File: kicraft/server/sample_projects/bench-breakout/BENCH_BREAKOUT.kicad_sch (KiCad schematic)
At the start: 0 parts

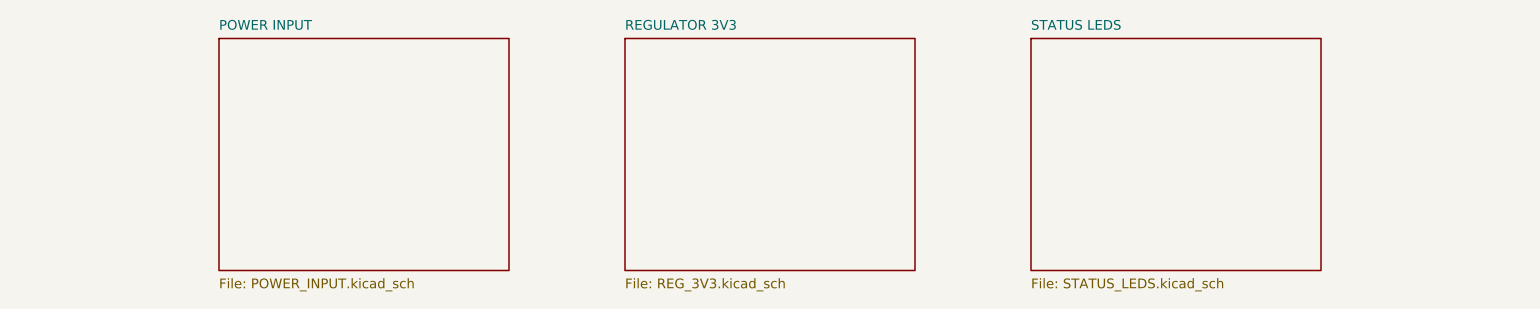
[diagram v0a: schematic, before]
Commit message: feat(showcase): refresh landing samples from self-eval 20260614
Promote the three best boards from self-eval batch 20260614T215540Z
(all grade B) into the landing-page showcase, replacing the regressed
PIR night light (D/45, hit erc_errors + unprogrammable_mcu gates):

- usb-pd-trigger (NEW, featured hero) — 81.0, fab-ready
- weather-sensor (re-promoted; stem A_BMP280_BAROMETRIC -> BMP280_QWIIC_USB_C)
- bench-breakout (re-promoted; 4->5 sheets, 16->19 parts)

Regenerated board.png/hero.png renders and interactive board.glb models
via scripts/promote_to_sample.py. Already live (deploy/restart-web.sh).

Co-Authored-By: Claude Opus 4.8 (1M context) <noreply@anthropic.com>
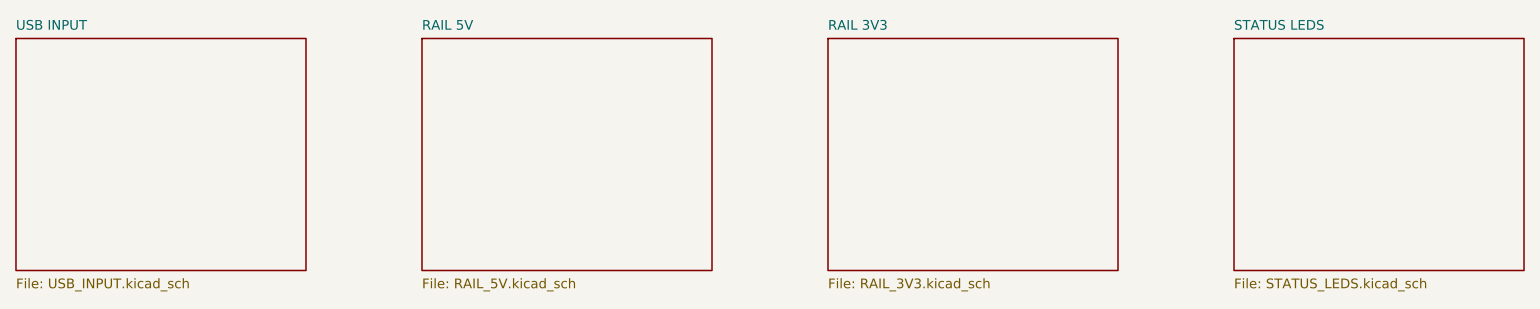
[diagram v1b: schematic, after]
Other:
- removed sheet POWER INPUT
- removed sheet REGULATOR 3V3
- added sheet RAIL 3V3 (RAIL_3V3.kicad_sch)
- added sheet RAIL 5V (RAIL_5V.kicad_sch)
- added sheet USB INPUT (USB_INPUT.kicad_sch)
- title: A bench breakout board that takes USB-C input and provides… -> A bench breakout board with USB-C input, regulated 3.3V and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
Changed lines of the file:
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@@
 	(paper "A4")
 	(title_block
-		(title "A bench breakout board that takes USB-C input and provides…")
+		(title "A bench breakout board with USB-C input, regulated 3.3V and…")
 		(rev "1.0")
 		(comment 1 "Generated by KiCraft pipeline")
 	)
 	(sheet
-		(at 66.04 90.17)
+		(at 39.37 90.17)
 		(size 38.1 30.48)
 		(exclude_from_sim no)
@@
 		(stroke (width 0.2) (type solid))
 		(fill (color 0 0 0 0.0000))
-		(property "Sheetname" "POWER INPUT"
-			(at 66.04 89.17 0)
+		(property "Sheetname" "USB INPUT"
+			(at 39.37 89.17 0)
 			(effects (font (size 1.27 1.27)) (justify left bottom))
 		)
-		(property "Sheetfile" "POWER_INPUT.kicad_sch"
-			(at 66.04 121.65 0)
+		(property "Sheetfile" "USB_INPUT.kicad_sch"
+			(at 39.37 121.65 0)
 			(effects (font (size 1.27 1.27)) (justify left top))
 		)
 		(instances
 			(project "BENCH_BREAKOUT"
-				(path "/" (page "POWER_INPUT"))
+				(path "/" (page "USB_INPUT"))
 			)
 		)
 	)
 	(sheet
-		(at 119.38 90.17)
+		(at 92.71 90.17)
 		(size 38.1 30.48)
 		(exclude_from_sim no)
@@
 		(stroke (width 0.2) (type solid))
 		(fill (color 0 0 0 0.0000))
-		(property "Sheetname" "REGULATOR 3V3"
-			(at 119.38 89.17 0)
+		(property "Sheetname" "RAIL 5V"
+			(at 92.71 89.17 0)
 			(effects (font (size 1.27 1.27)) (justify left bottom))
 		)
-		(property "Sheetfile" "REG_3V3.kicad_sch"
-			(at 119.38 121.65 0)
+		(property "Sheetfile" "RAIL_5V.kicad_sch"
+			(at 92.71 121.65 0)
 			(effects (font (size 1.27 1.27)) (justify left top))
 		)
 		(instances
 			(project "BENCH_BREAKOUT"
-				(path "/" (page "REG_3V3"))
+				(path "/" (page "RAIL_5V"))
 			)
 		)
 	)
 	(sheet
-		(at 172.72 90.17)
+		(at 146.05 90.17)
+		(size 38.1 30.48)
+		(exclude_from_sim no)
+		(in_bom yes)
+		(on_board yes)
+		(dnp no)
+		(fields_autoplaced yes)
+		(stroke (width 0.2) (type solid))
+		(fill (color 0 0 0 0.0000))
+		(property "Sheetname" "RAIL 3V3"
+			(at 146.05 89.17 0)
+			(effects (font (size 1.27 1.27)) (justify left bottom))
+		)
+		(property "Sheetfile" "RAIL_3V3.kicad_sch"
+			(at 146.05 121.65 0)
+			(effects (font (size 1.27 1.27)) (justify left top))
+		)
+		(instances
+			(project "BENCH_BREAKOUT"
+				(path "/" (page "RAIL_3V3"))
+			)
+		)
+	)
+	(sheet
+		(at 199.39 90.17)
 		(size 38.1 30.48)
 		(exclude_from_sim no)
@@
 		(fill (color 0 0 0 0.0000))
 		(property "Sheetname" "STATUS LEDS"
-			(at 172.72 89.17 0)
+			(at 199.39 89.17 0)
 			(effects (font (size 1.27 1.27)) (justify left bottom))
 		)
 		(property "Sheetfile" "STATUS_LEDS.kicad_sch"
-			(at 172.72 121.65 0)
+			(at 199.39 121.65 0)
 			(effects (font (size 1.27 1.27)) (justify left top))
 		)
